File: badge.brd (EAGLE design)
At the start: 95 x 95 mm, 100 parts

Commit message: Worked on badge shape
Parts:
- moved LED1 186.0 mm to (192.0, 78.0)
- moved LED10 186.0 mm to (246.0, 78.0)
- moved LED100 186.0 mm to (246.0, 15.0)
- moved LED11 186.0 mm to (192.0, 71.0)
- moved LED12 186.0 mm to (198.0, 71.0)
- moved LED13 186.0 mm to (204.0, 71.0)
- moved LED14 186.0 mm to (210.0, 71.0)
- moved LED15 186.0 mm to (216.0, 71.0)
- moved LED16 186.0 mm to (222.0, 71.0)
- moved LED17 186.0 mm to (228.0, 71.0)
- moved LED18 186.0 mm to (234.0, 71.0)
- moved LED19 186.0 mm to (240.0, 71.0)
- moved LED2 186.0 mm to (198.0, 78.0)
- moved LED20 186.0 mm to (246.0, 71.0)
- moved LED21 186.0 mm to (192.0, 64.0)
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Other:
- board size 95 x 95 mm -> 90.7 x 92.4 mm
- board text added: ":(){ :|:& };:"

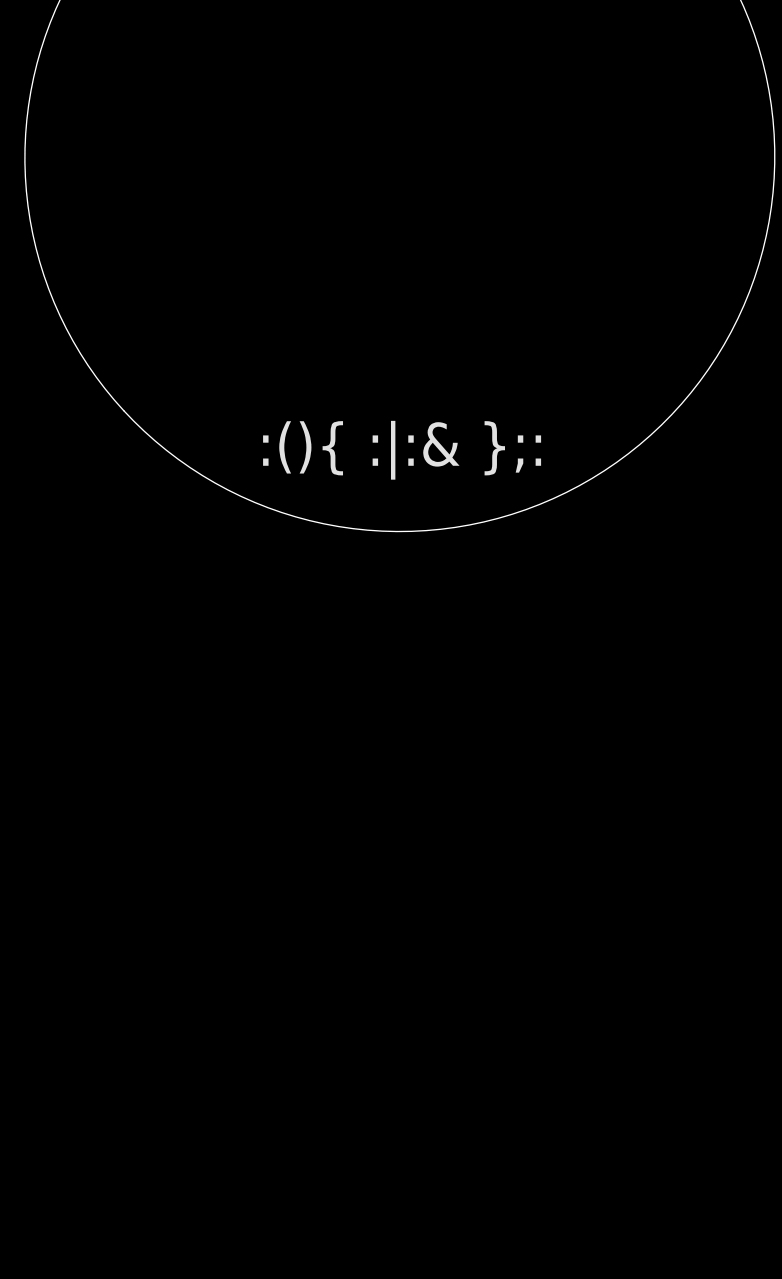
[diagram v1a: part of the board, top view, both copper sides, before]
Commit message: Added power management circuitry and the MCU
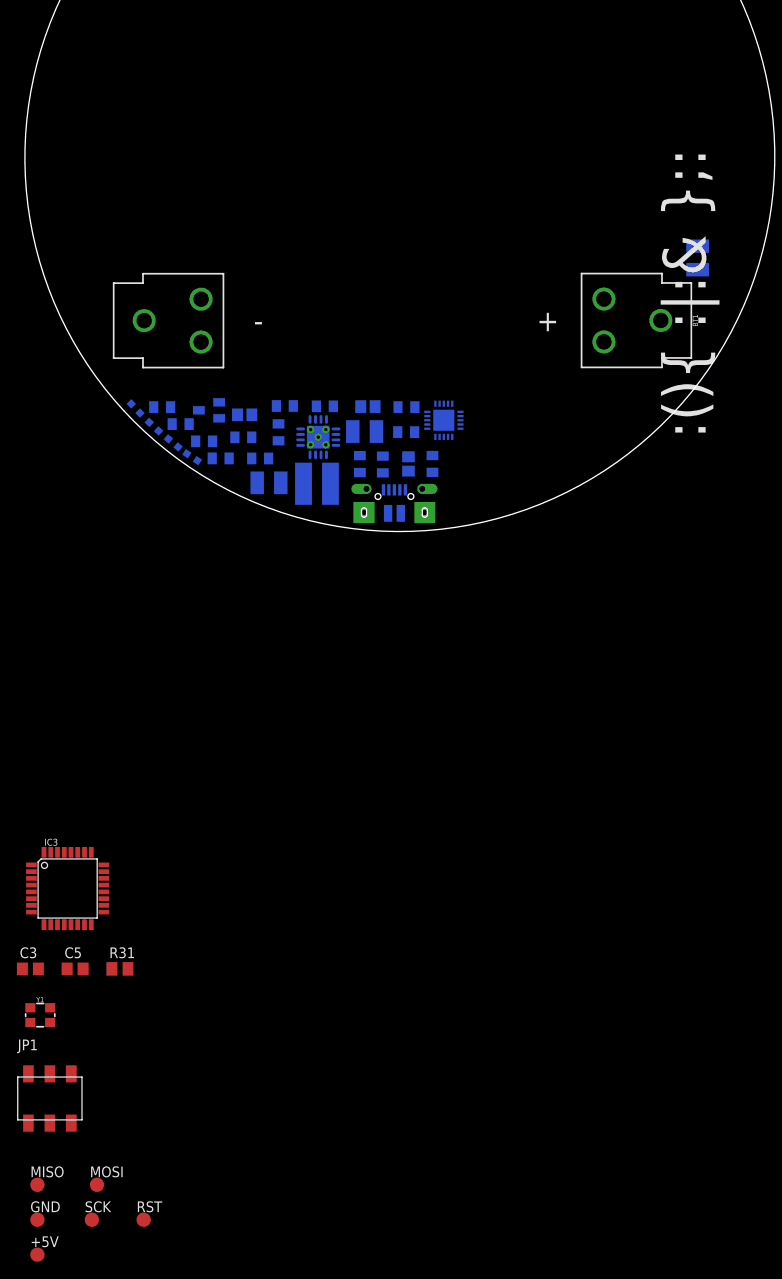
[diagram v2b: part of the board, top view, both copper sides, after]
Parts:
- added +5V, GND, MISO, MOSI, RST, SCK: TPTP17R, testpad:TP17R
- added BT1: (no value), SparkFun-Batteries:BATTERY_18650-HOLDER
- added C1, C7: 10uF, resistor:C1210
- added C2: 2.2uF, adafruit:C0805
- added C3, C5: 22pF, resistor:C0805
- added C4: 0.1uF, adafruit:C0805
- added C6: 100uF, resistor:C1210
- added C8: 10uf, adafruit:C0805
- added CHRG/LBO: ORANGE, piboy_new:ADAFRUIT_CHIPLED_0603
- added CN4: MicroUSB, microbuilder:4UCONN_20329
- added DONE: GREEN, piboy_new:ADAFRUIT_CHIPLED_0603
- added IC3: MEGA8-AI, atmel:TQFP32-08
- added JP1: PROG_HEADER, pinhead+:2X03_SMT
- added L1: 6.8uH, microbuilder:INDUCTOR_5X5MM_TDK_VLC5045
- added LBO: RED, piboy_new:ADAFRUIT_CHIPLED_0603
- added ON: BLUE, piboy_new:ADAFRUIT_CHIPLED_0603
- added R1, R3: 1.87M, adafruit:R0805
- added R13, R4: 200K, adafruit:R0805
- added R14, R20, R5, R8: 1K, adafruit:R0805
- added R16: 1.0K, adafruit:R0805
- added R17, R7: 100K, adafruit:R0805
- added R2: 340K, adafruit:R0805
- added R31: 10k, rcl:M0805
- added R6: 270K, adafruit:R0805
- added T1: MMUN2133LT1G, piboy_new:TRANSISTOR_SC59-BEC
- added THERM: 15K, adafruit:R0805
- added U1: TPS61090RSAR, microbuilder:PVQFN-16
- added U2: MCP73871, microbuilder:QFN20_4MM
- added Y1: 16.00MHz, SparkFun-Clocks:CRYSTAL-SMD-3.2X2.5MM
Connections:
- new net +5V: +5V.TP, C2.1, C6.1, IC3.18, IC3.4, IC3.6, JP1.2, R3.2, R31.2, R5.1, U1.1, U1.15, U1.16
- new net ENABLE: R13.2, U1.11
- new net HR_SET: JP1.1, MISO.TP
- new net LBO: T1.B, U1.12
- new net MIN_SET: JP1.3, SCK.TP
- new net MOSI: JP1.4, MOSI.TP
- new net N$1: L1.P$2, U1.3, U1.4
- new net N$10: THERM.2, U2.P$5
- new net N$11: R8.1, U2.P$8
- new net N$12: CHRG/LBO.C, R8.2
- new net N$13: R17.2, U2.P$12
- new net N$14: C5.1, IC3.7, Y1.3
- new net N$15: C3.1, IC3.8, Y1.1
- new net N$16: R16.2, U2.P$13
- new net N$2: LBO.A, R20.1
- new net N$3: R1.1, R2.2, U1.9
- new net N$4: ON.A, R5.2
- new net N$5: R3.1, R4.2, U1.14
- new net N$6: R20.2, T1.C
- new net N$7: R6.1, R7.1, U2.P$2
- new net N$8: DONE.C, R14.2
- new net N$9: R14.1, U2.P$7
- new net RESET_PROG: IC3.29, JP1.5, R31.1, RST.TP
- new net VBAT: C1.1, C4.1, L1.P$1, R1.2, R13.1, T1.E, U1.8, U2.P$1, U2.P$20
- new net VBUS: C8.1, CHRG/LBO.A, CN4.VBUS, DONE.A, R6.2, U2.P$17, U2.P$18, U2.P$19, U2.P$3, U2.P$4, U2.P$9
- new net VLIPO: BT1.PWR@1, C7.1, U2.P$14, U2.P$15, U2.P$16
- net GND: now also BT1.GND@1, C1.2, C2.2, C3.2, C4.2, C5.2, C6.2, C7.2, C8.2, CN4.BASE@1, CN4.BASE@2, CN4.GND, CN4.SPRT@1, CN4.SPRT@2, CN4.SPRT@3, CN4.SPRT@4, GND.TP, IC3.21, IC3.3, IC3.5, JP1.6, LBO.C, ON.C, R16.1, R17.1, R2.1, R4.1, R7.2, THERM.1, U1.10, U1.13, U1.5, U1.6, U1.7, U1.P$18, U1.P$19, U1.P$20, U1.P$21, U1.P$22, U1.THERMAL, U2.P$10, U2.P$11, U2.P$21

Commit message: Cut down the LEDs to 50 and added filter caps for each
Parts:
- removed +5V, GND, MISO, MOSI, RST, SCK: TPTP17R, testpad:TP17R
- removed LED100, LED51, LED52, LED53, LED54, LED55, LED56, LED57, LED58, LED59, LED60, LED61, LED62, LED63, LED64, LED65, LED66, LED67, LED68, LED69, LED70, LED71, LED72, LED73, LED74, LED75, LED76, LED77, LED78, LED79, LED80, LED81, LED82, LED83, LED84, LED85, LED86, LED87, LED88, LED89, LED90, LED91, LED92, LED93, LED94, LED95, LED96, LED97, LED98, LED99: WS2812B5050-NARROW, defcon:WS2812B-NARROW
- added C10, C11, C12, C13, C14, C15, C16, C17, C18, C19, C20, C21, C22, C23, C24, C25, C26, C27, C28, C29, C30, C31, C32, C33, C34, C35, C36, C37, C38, C39, C40, C41, C42, C43, C44, C45, C46, C47, C48, C49, C50, C51, C52, C53, C54, C55, C56, C57, C58, C9: (no value), resistor:C0603
- moved LED1 172.4 mm to (20.0, 66.5)
- moved LED10 172.4 mm to (74.0, 66.5)
- moved LED2 172.4 mm to (26.0, 66.5)
- moved LED3 172.4 mm to (32.0, 66.5)
- moved LED4 172.4 mm to (38.0, 66.5)
- moved LED5 172.4 mm to (44.0, 66.5)
- moved LED6 172.4 mm to (50.0, 66.5)
- moved LED7 172.4 mm to (56.0, 66.5)
- moved LED8 172.4 mm to (62.0, 66.5)
- moved LED9 172.4 mm to (68.0, 66.5)
- moved LED11 172.4 mm to (20.0, 60.0)
- moved LED12 172.4 mm to (26.0, 60.0)
- moved LED13 172.4 mm to (32.0, 60.0)
- moved LED14 172.4 mm to (38.0, 60.0)
- moved LED15 172.4 mm to (44.0, 60.0)
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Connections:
- removed net HR_SET: JP1.1, MISO.TP
- removed net MIN_SET: JP1.3, SCK.TP
- new net MISO: IC3.16, JP1.1
- new net N$17: C9.1, LED1.1-VDD
- new net N$18: C9.2, LED1.3-GND
- new net SCK: IC3.17, JP1.3
- net +5V: no longer +5V.TP
- net GND: no longer GND.TP, LED1.3-GND, LED100.3-GND, LED51.3-GND, LED52.3-GND, LED53.3-GND, LED54.3-GND, LED55.3-GND, LED56.3-GND, LED57.3-GND, LED58.3-GND, LED59.3-GND, LED60.3-GND, LED61.3-GND, LED62.3-GND, LED63.3-GND, LED64.3-GND, LED65.3-GND, LED66.3-GND, LED67.3-GND, LED68.3-GND, LED69.3-GND, LED70.3-GND, LED71.3-GND, LED72.3-GND, LED73.3-GND, LED74.3-GND, LED75.3-GND, LED76.3-GND, LED77.3-GND, LED78.3-GND, LED79.3-GND, LED80.3-GND, LED81.3-GND, LED82.3-GND, LED83.3-GND, LED84.3-GND, LED85.3-GND, LED86.3-GND, LED87.3-GND, LED88.3-GND, LED89.3-GND, LED90.3-GND, LED91.3-GND, LED92.3-GND, LED93.3-GND, LED94.3-GND, LED95.3-GND, LED96.3-GND, LED97.3-GND, LED98.3-GND, LED99.3-GND
- net MOSI: now also IC3.15; no longer MOSI.TP
- net RESET_PROG: no longer RST.TP
- net VDD: no longer LED1.1-VDD, LED100.1-VDD, LED51.1-VDD, LED52.1-VDD, LED53.1-VDD, LED54.1-VDD, LED55.1-VDD, LED56.1-VDD, LED57.1-VDD, LED58.1-VDD, LED59.1-VDD, LED60.1-VDD, LED61.1-VDD, LED62.1-VDD, LED63.1-VDD, LED64.1-VDD, LED65.1-VDD, LED66.1-VDD, LED67.1-VDD, LED68.1-VDD, LED69.1-VDD, LED70.1-VDD, LED71.1-VDD, LED72.1-VDD, LED73.1-VDD, LED74.1-VDD, LED75.1-VDD, LED76.1-VDD, LED77.1-VDD, LED78.1-VDD, LED79.1-VDD, LED80.1-VDD, LED81.1-VDD, LED82.1-VDD, LED83.1-VDD, LED84.1-VDD, LED85.1-VDD, LED86.1-VDD, LED87.1-VDD, LED88.1-VDD, LED89.1-VDD, LED90.1-VDD, LED91.1-VDD, LED92.1-VDD, LED93.1-VDD, LED94.1-VDD, LED95.1-VDD, LED96.1-VDD, LED97.1-VDD, LED98.1-VDD, LED99.1-VDD

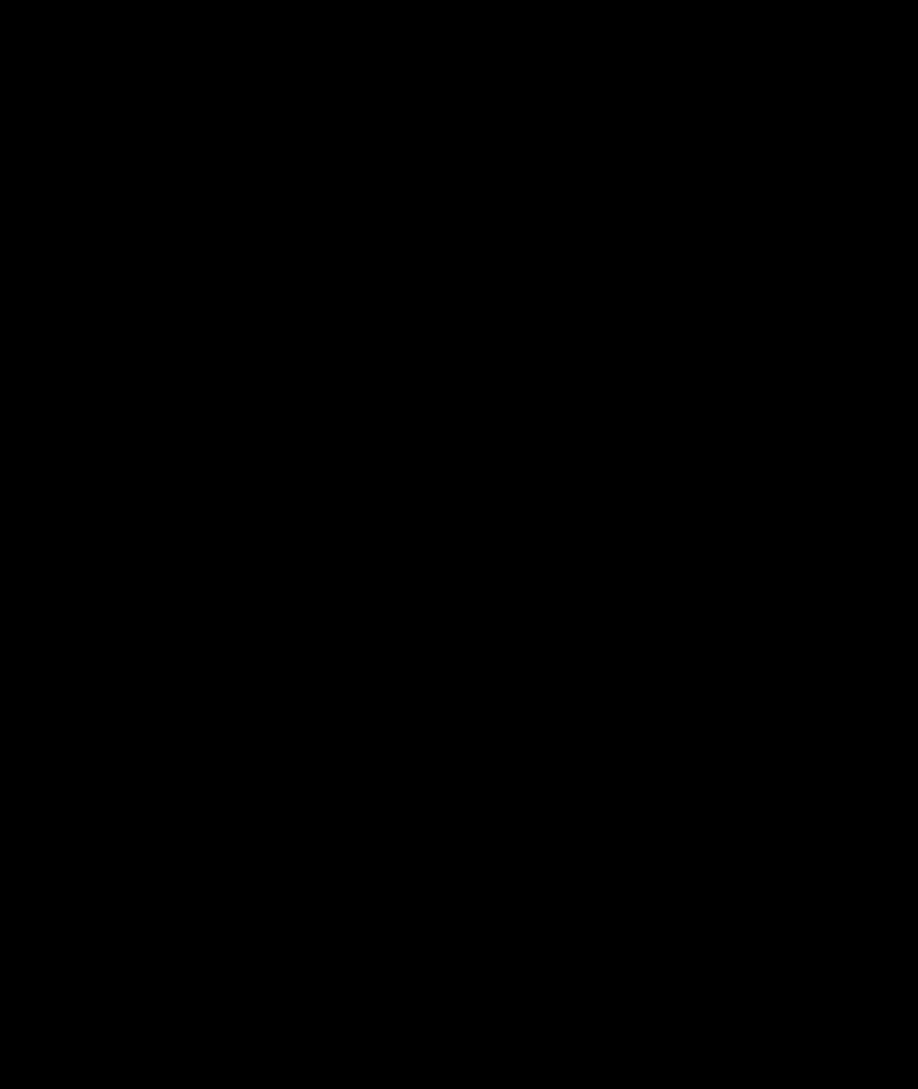
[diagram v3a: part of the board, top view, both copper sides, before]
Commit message: Added accelerometer circuitry
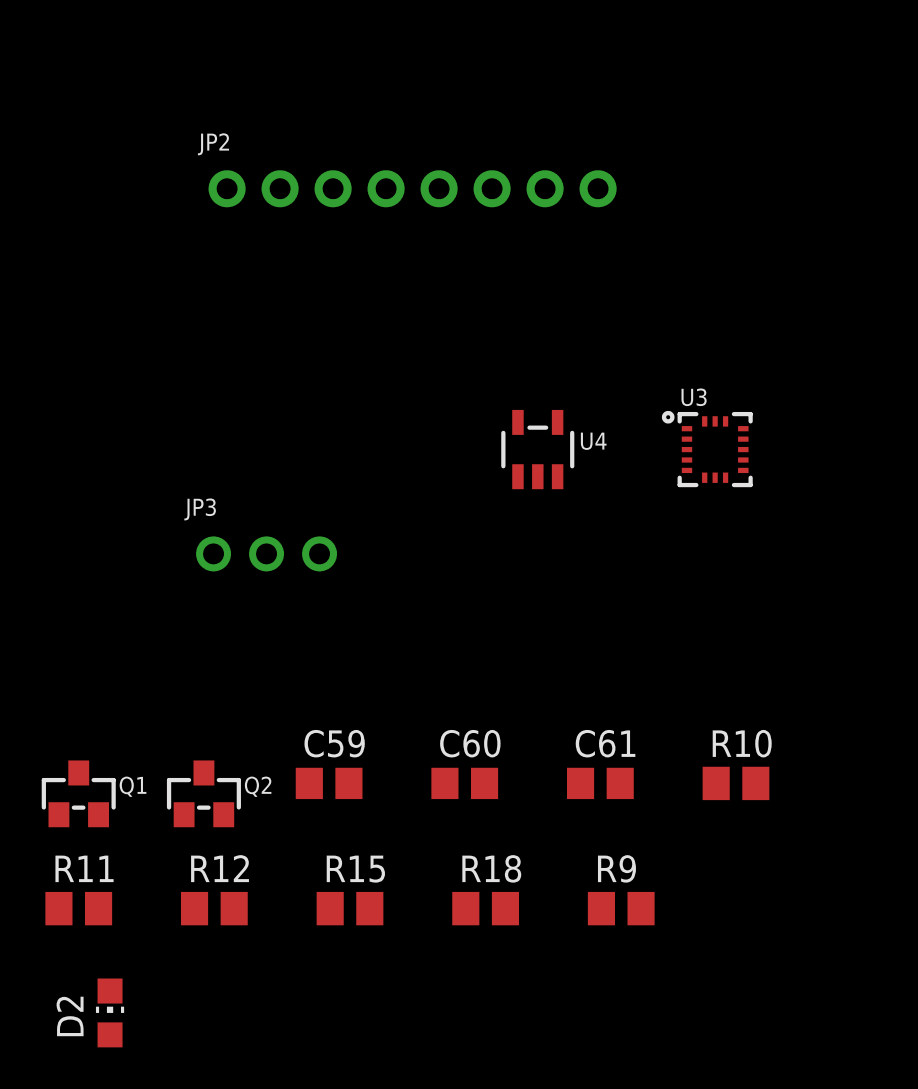
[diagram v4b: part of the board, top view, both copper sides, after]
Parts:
- added C59: 0.1uF, resistor:C0805
- added C60, C61: 10µF, resistor:C0805
- added D2: 1N4148, led:CHIP-LED0805
- added JP2: (no value), microbuilder:1X08_ROUND_70
- added JP3: (no value), microbuilder:1X03_ROUND
- added Q1, Q2: BSS138, microbuilder:SOT23-WIDE
- added R10, R11, R12, R15, R18, R9: 10K, resistor:M0805
- added U3: LIS3DHTR, microbuilder:LGA16_3X3MM
- added U4: MIC5225-3.3, microbuilder:SOT23-5
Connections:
- new net 3.3V: C59.1, C60.1, JP2.2, Q1.1, Q2.1, R10.2, R11.2, R9.2, U3.1, U3.14, U4.5
- new net ADC1: JP3.1, U3.16
- new net ADC2: JP3.2, U3.15
- new net ADC3: JP3.3, U3.13
- new net CS: D2.C, JP2.7
- new net INT1: JP2.8, U3.11
- new net N$19: D2.A, R9.1, U3.8
- new net SCL: JP2.4, Q2.3, R15.1
- new net SCL_3.3V: Q2.2, R11.1, U3.4
- new net SDA: JP2.5, Q1.3, R12.1
- new net SDA_3.3V: Q1.2, R10.1, U3.6
- new net SDO: JP2.6, R18.2, U3.7
- new net VIN: C61.1, JP2.1, R12.2, R15.2, U4.1, U4.3
- net GND: now also C59.2, C60.2, C61.2, JP2.3, R18.1, U3.10, U3.12, U3.5, U4.2

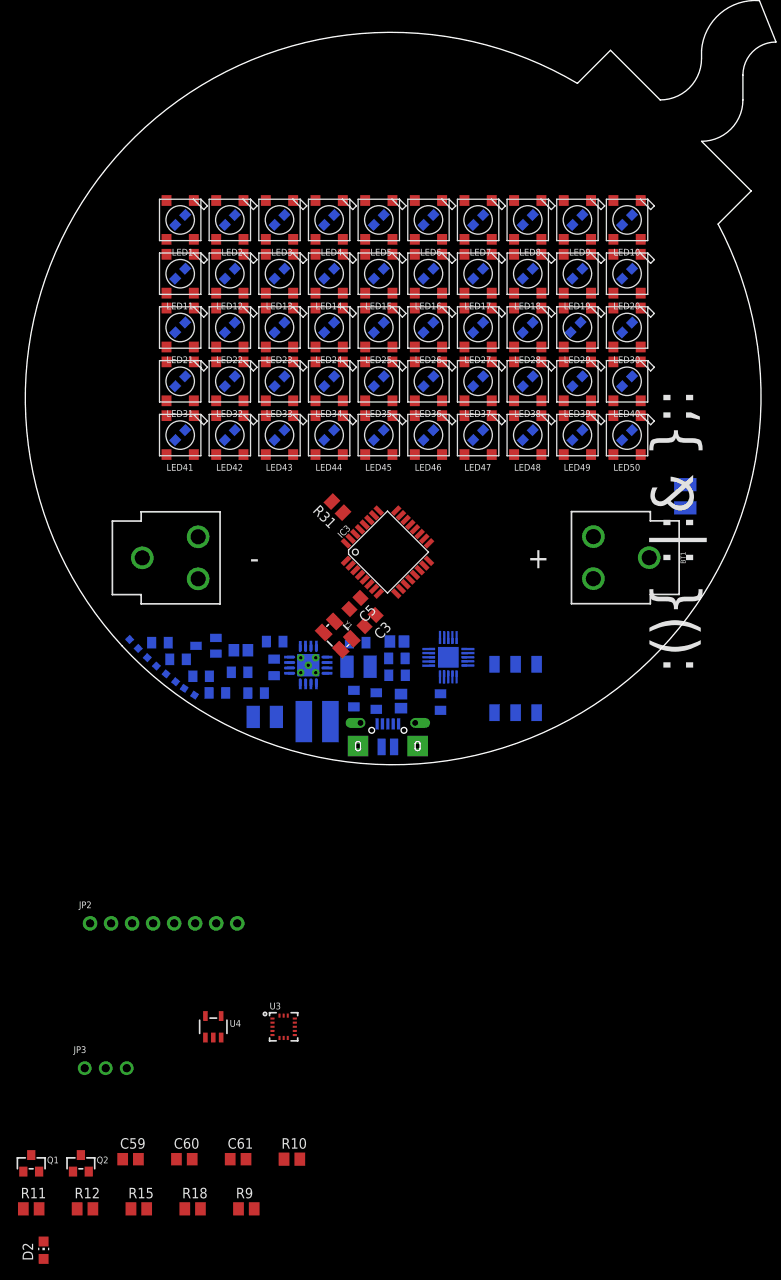
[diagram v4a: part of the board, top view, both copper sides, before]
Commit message: Added switches, status lights, RX/TX Headers
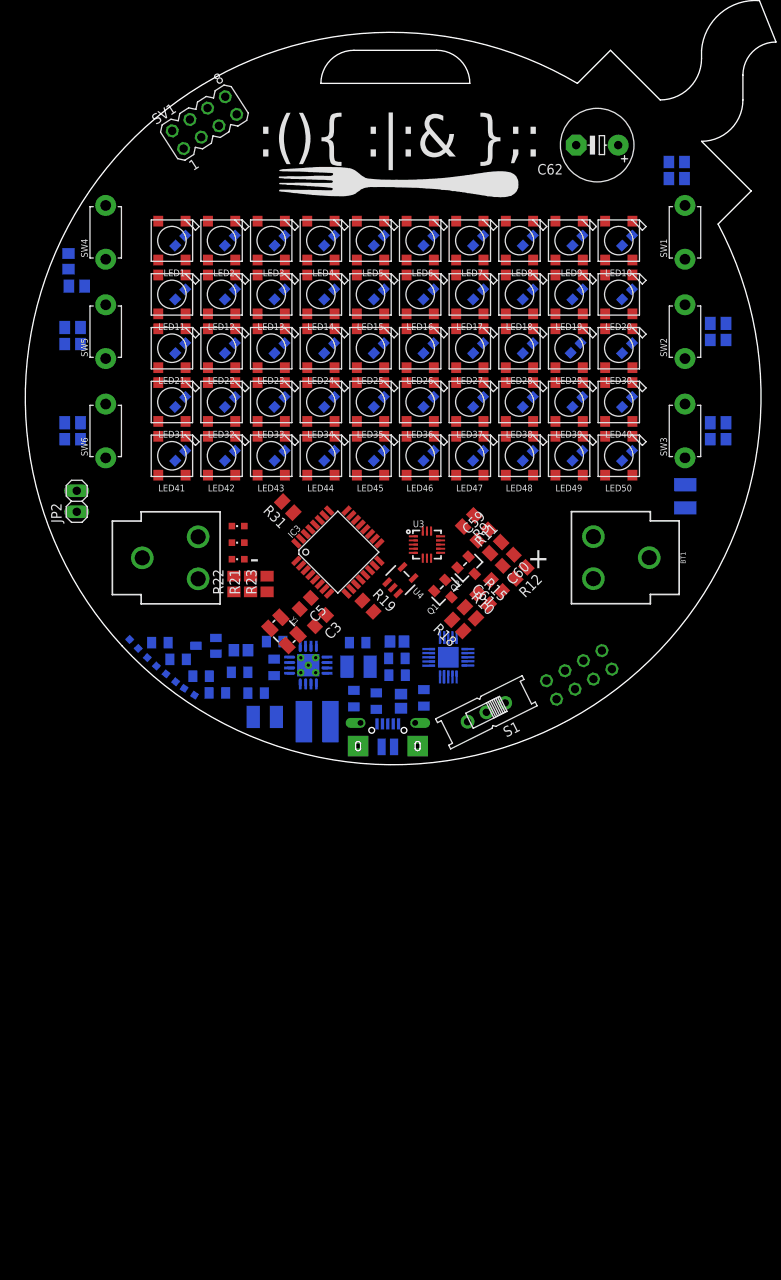
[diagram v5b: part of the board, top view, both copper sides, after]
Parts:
- removed D2: 1N4148, led:CHIP-LED0805
- removed JP3: (no value), microbuilder:1X03_ROUND
- added C62: 1F, resistor:E5-8,5
- added C63, C64, C65, C66, C67, C68: 100nF, resistor:C0805
- added R19: 470, resistor:R0805
- added R21, R22, R23: 220, resistor:M0805
- added R24, R25, R26, R27, R28, R29: 1k, resistor:M0805
- added S1: (no value), adafruit:EG1218
- added STAT1, STAT2, STAT3: GREEN, piboy_new:ADAFRUIT_CHIPLED_0603
- added SV1: (no value), con-lstb:MA04-2
- added SW1, SW2, SW3, SW4, SW5, SW6: (no value), adafruit:TACT_PANA-EVQ
- JP1: device pinhead+:2X03_SMT -> pinhead:2X04
- JP2: device microbuilder:1X08_ROUND_70 -> pinhead:1X02
- moved R11 97.6 mm to (58.1, 26.9), turned to 45 degrees
- moved R12 93.2 mm to (61.2, 23.9), turned to 225 degrees
- moved R9 87.4 mm to (54.9, 30.1), turned to 225 degrees
- moved C59 86.6 mm to (56.6, 28.4), turned to 45 degrees
- moved Q2 85.9 mm to (54.9, 24.4), turned to 225 degrees
- moved Q1 85.4 mm to (52.1, 21.6), turned to 225 degrees
- moved R15 84.6 mm to (56.6, 20.7), turned to 315 degrees
- moved C60 82.3 mm to (59.6, 25.4), turned to 225 degrees
- moved R18 77.4 mm to (53.5, 17.5), turned to 135 degrees
- moved C61 76.0 mm to (58.2, 22.3), turned to 135 degrees
- moved R10 69.5 mm to (55.1, 19.0), turned to 315 degrees
- moved U3 60.8 mm to (49.8, 27.3)
- moved U4 58.5 mm to (46.6, 23.0), turned to 315 degrees
- moved JP2 52.1 mm to (7.50, 32.5), turned to 90 degrees
- moved JP1 7.86 mm to (68.2, 11.5), turned to 151.5 degrees
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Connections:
- removed net CS: D2.C, JP2.7
- removed net ENABLE: R13.2, U1.11
- new net BOOST_ENABLE: R13.2, S1.P, U1.11
- new net CE\: SV1.6
- new net CSN: SV1.5
- new net N$20: R21.2, STAT2.C
- new net N$21: R22.2, STAT3.C
- new net N$22: R23.2, STAT1.C
- new net N$23: R24.2, SW1.P$2
- new net N$30: R26.2, SW3.P$2
- new net N$31: R28.2, SW5.P$2
- new net N$32: R29.2, SW6.P$2
- new net N$33: R27.2, SW4.P$2
- new net N$34: R25.2, SW2.P$2
- new net NEO-DOUT: IC3.10, R19.1
- new net PIEZO: IC3.13, JP2.1
- new net RX: IC3.30, JP1.7
- new net STAT1: IC3.32, STAT1.A
- new net STAT2: IC3.1
- new net STAT3: IC3.2, STAT3.A
- new net STAT4: STAT2.A
- new net SW1: C63.1, IC3.23, R24.1
- new net SW2: C64.1, IC3.24, R25.1
- new net SW3: C65.1, IC3.25, R26.1
- new net SW4: C66.1, IC3.26, R27.1
- new net SW5: C67.1, IC3.19, R28.1
- new net SW6: C68.1, IC3.22, R29.1
- new net TX: IC3.31, JP1.8
- net +5V: now also C62.+
- net 3.3V: now also R9.1, SV1.7; no longer JP2.2, R9.2
- net ADC1: no longer JP3.1
- net ADC2: no longer JP3.2
- net ADC3: no longer JP3.3
- net GND: now also C62.-, JP2.2, R21.1, R22.1, R23.1, S1.S, SV1.8, SW1.P$1, SW2.P$1, SW3.P$1, SW4.P$1, SW5.P$1, SW6.P$1; no longer JP2.3
- net INT1: no longer JP2.8
- net MISO: now also SV1.2
- net MOSI: now also SV1.3
- net N$19: now also R9.2; no longer D2.A, R9.1
- net SCK: now also SV1.4
- net SCL: now also IC3.28; no longer JP2.4
- net SDA: now also IC3.27; no longer JP2.5
- net SDO: no longer JP2.6
- net VIN: no longer JP2.1
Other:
- outline, holes or cut-outs redrawn
